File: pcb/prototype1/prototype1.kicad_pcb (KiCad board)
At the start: 2 copper layers, 95.1 x 95 mm, 98 parts, among them P1 AAA1 HOT, P2 AAA1 GND, P3 AAA2 GND, P4 AAA2 HOT, P5 USB_B, SW1 SPST, SW2 Button, SW3 Button, SW4 Button, SW5 Button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

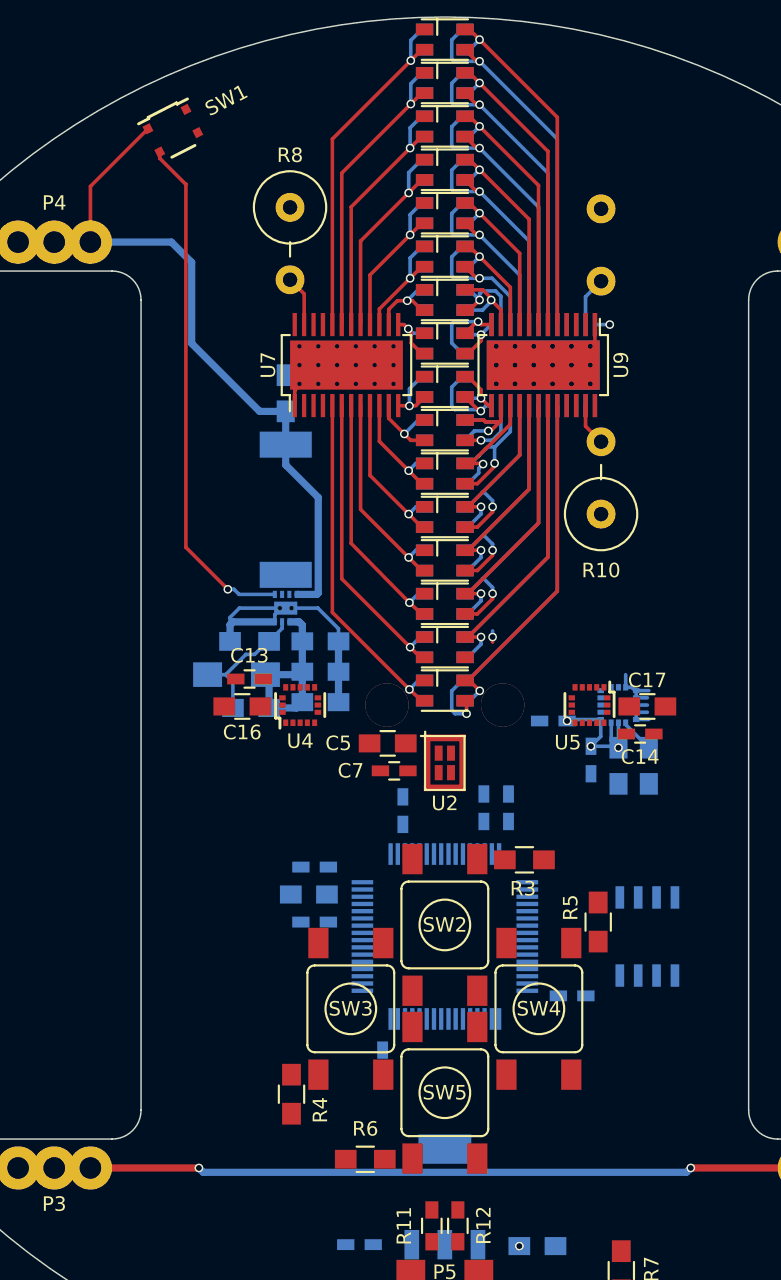
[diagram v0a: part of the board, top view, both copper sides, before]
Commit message: Change pcb layout a bit
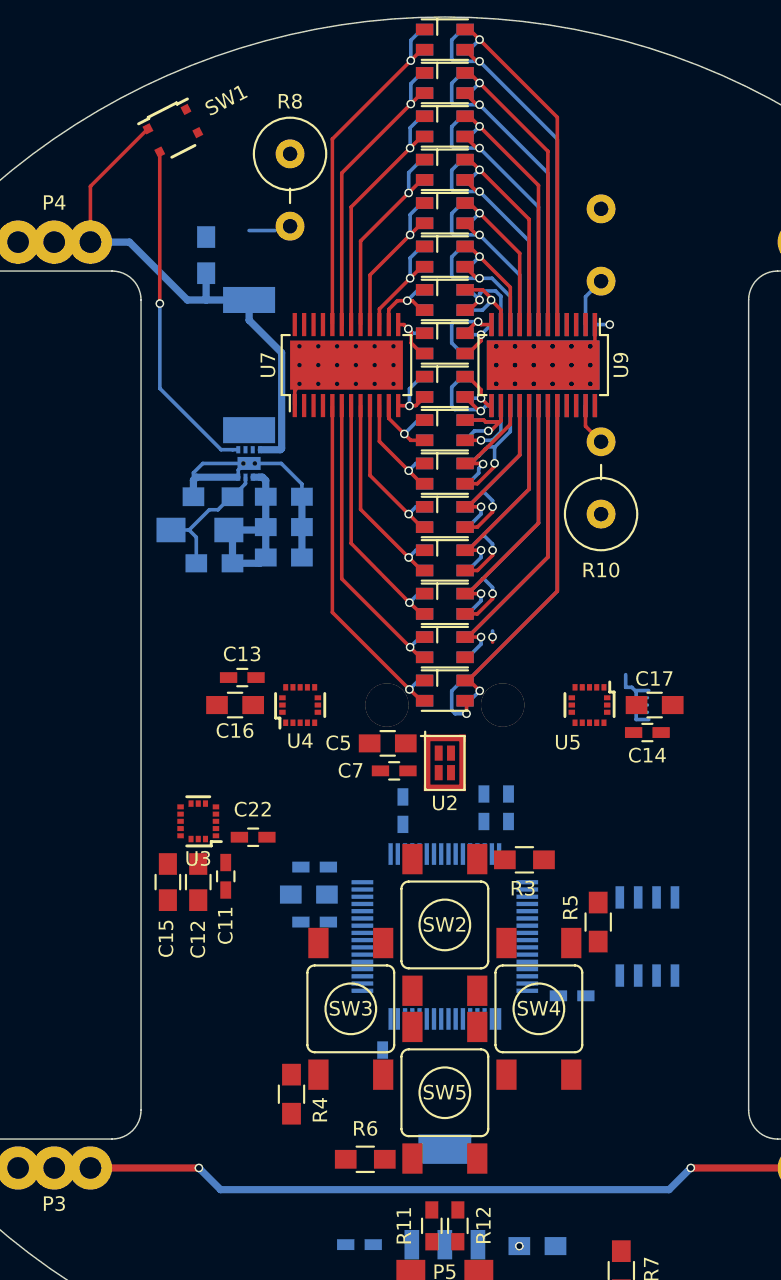
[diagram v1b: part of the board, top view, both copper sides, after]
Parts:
- C11, C12, C15, C22, U3: moved to F.Cu
- moved C15 34.2 mm to (130.9, 112.2)
- moved C12 30.1 mm to (133.0, 112.2)
- moved U3 30.1 mm to (133.0, 108.0), turned to 180 degrees
- moved C11 26.5 mm to (134.9, 111.8)
- moved C22 22.3 mm to (136.8, 109.1), turned to 0 degrees
- moved C23 11.0 mm to (133.5, 68.9)
- moved C18 10.3 mm to (134.1, 90.2)
- moved C19 10.3 mm to (138.9, 85.6)
- moved C20 10.3 mm to (138.9, 87.7)
- moved C21 10.3 mm to (138.9, 89.8)
- moved L1 10.3 mm to (136.5, 76.5)
- moved R1 10.3 mm to (133.1, 87.9)
- moved R2 10.3 mm to (134.0, 85.6)
- moved U6 10.3 mm to (136.5, 83.3)
- moved R8 3.70 mm to (139.3, 64.4)
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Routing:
- net Net-(SW1-Pad2): track 35.6 -> 23.5 mm
- net +3V3: track 25.0 -> 15.0 mm, vias 5 -> 2
- net Net-(C23-Pad2): track 45.9 -> 36.7 mm
- net Net-(R8-Pad2): track 3.50 -> 0.00 mm
- net Net-(C15-Pad1): track 2.39 -> 0.00 mm
- net Net-(P1-Pad1): track 49.2 -> 50.2 mm

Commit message: Connected many things on pcb
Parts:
- U11: footprint TO_SOT_Packages_SMD:SOT-223 -> spin:SOT-223
- moved R9 4.94 mm to (164.4, 64.9)
- moved R10 3.68 mm to (163.4, 86.9)
- moved R11 0.50 mm to (149.1, 135.5)
- moved R12 0.50 mm to (150.9, 135.5)
- turned R6 to 180 degrees
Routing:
- net LED_TOG: track 0.00 -> 191.4 mm, vias 0 -> 15
- net MISO1: track 0.47 -> 143.2 mm, vias 0 -> 11
- net SCK1: track 0.95 -> 139.7 mm, vias 0 -> 15
- net +3V3: track 15.0 -> 143.7 mm, vias 2 -> 38
- net MOSI1: track 0.48 -> 122.0 mm, vias 0 -> 11
- net SS_GREEN: track 0.00 -> 109.2 mm, vias 0 -> 11
- net SS_BLUE: track 0.00 -> 100.3 mm, vias 0 -> 12
- net SS_RED: track 0.00 -> 64.5 mm, vias 0 -> 5
- net GND: track 40.4 -> 81.2 mm, vias 2 -> 28
- net USB_DM: track 0.00 -> 28.5 mm, vias 0 -> 1
- net USB_DP: track 0.00 -> 23.8 mm, vias 0 -> 1
- net LED1: track 0.00 -> 21.0 mm, vias 0 -> 1
- net SS_GYRO: track 0.00 -> 20.0 mm, vias 0 -> 3
- net BUT2: track 0.00 -> 18.0 mm, vias 0 -> 3
- net SS_ACC2: track 0.00 -> 15.9 mm, vias 0 -> 3
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
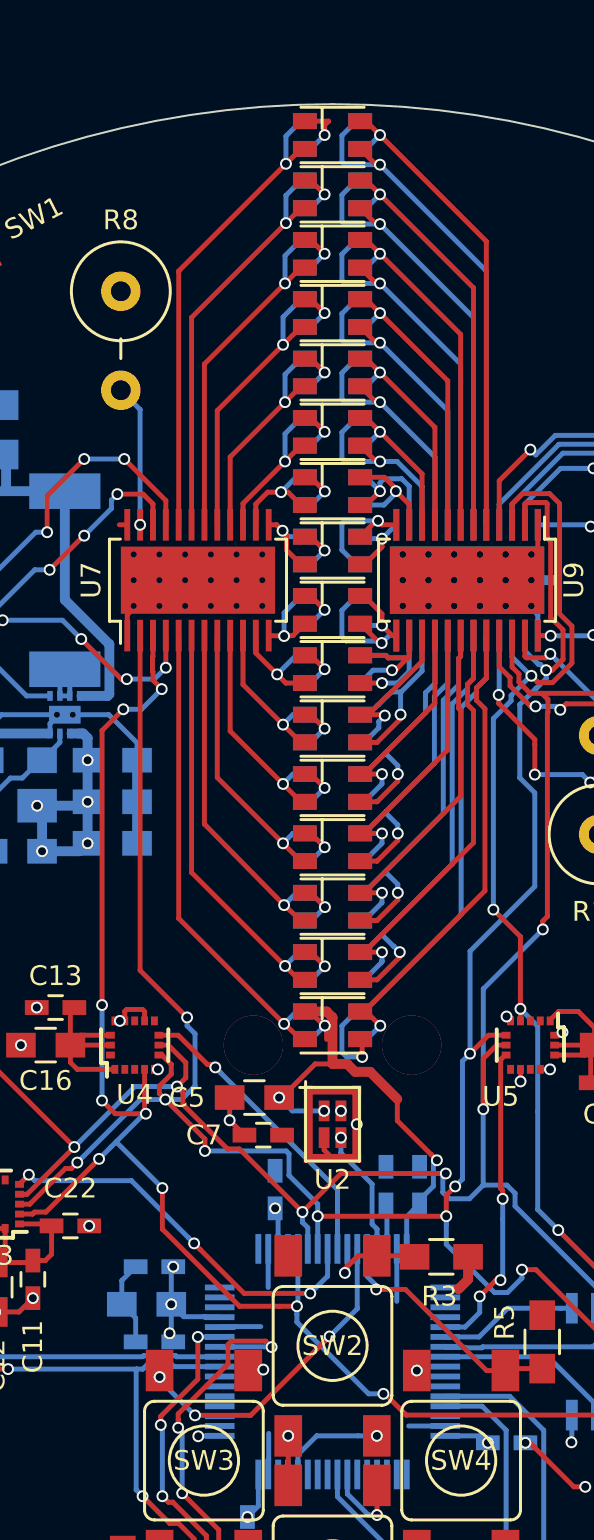
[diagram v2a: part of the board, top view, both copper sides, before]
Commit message: swap a couple pins on stm32
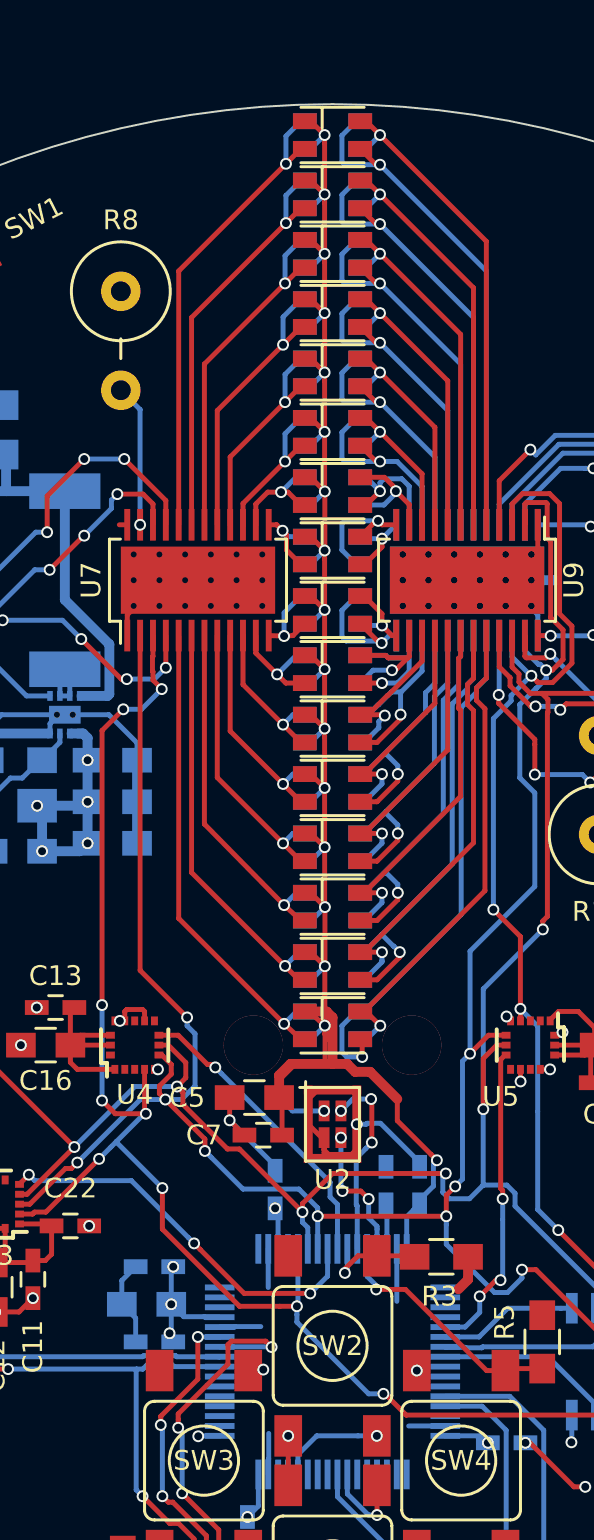
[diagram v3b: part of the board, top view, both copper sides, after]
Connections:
- U1 pad 27: BUT2 -> MIC_DATA
- U1 pad 51: MIC_DATA -> Net-(U1-Pad51)
- U1 pad 62: Net-(U1-Pad62) -> BUT2
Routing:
- net +3V3: track 143.7 -> 196.6 mm, vias 38 -> 37
- net GND: track 81.2 -> 98.2 mm
- net BUT2: track 18.0 -> 1.86 mm, vias 3 -> 0
- net MIC_DATA: track 0.00 -> 9.75 mm, vias 1 -> 3
- net MOSI1: track 122.0 -> 121.3 mm
- net MIC_CLK: track 6.38 -> 6.92 mm, vias 1 -> 3

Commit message: pcb is connected!
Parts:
- added H10: Hole, spin:Zip-tie-slot, F.Cu at (186.0, 100.0)
- added H7: Hole, spin:Zip-tie-slot, F.Cu at (132.0, 100.0)
- added H8: Hole, spin:Zip-tie-slot, F.Cu at (113.9, 100.0)
- added H9: Hole, spin:Zip-tie-slot, F.Cu at (168.0, 100.0)
- SW2, SW3, SW4, SW5: value Button -> SPST_two_terminals
- turned R3 to 180 degrees
- turned R4 to 90 degrees
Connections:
- R3 pad 1: BOOT0 -> +3V3
- R3 pad 2: +3V3 -> BUT1
- R4 pad 1: BUT2 -> +3V3
- R4 pad 2: +3V3 -> BUT2
- R6 pad 1: BUT4 -> Net-(R6-Pad1)
- SW2 pad 1: BOOT0 -> BUT1
- SW2 pad 2: GND -> BOOT0
- SW3 pad 2: GND -> Net-(SW3-Pad2)
- SW4 pad 2: GND -> Net-(SW4-Pad2)
- SW5 pad 2: GND -> Net-(R6-Pad1)
- U1 pad 26: BOOT0 -> BUT1
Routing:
- net GND: track 98.2 -> 145.5 mm, vias 28 -> 35
- net +3V3: track 196.6 -> 224.5 mm, vias 37 -> 38
- net BUT2: track 1.86 -> 12.1 mm, vias 0 -> 3
- net Net-(P1-Pad1): track 50.2 -> 60.2 mm
- net Net-(C23-Pad2): track 36.7 -> 46.5 mm
- net BUT4: track 12.5 -> 2.84 mm
- net Net-(R6-Pad1): track 0.00 -> 8.04 mm
- net BOOT0: track 10.7 -> 5.38 mm, vias 2 -> 1
- net BUT1: track 0.00 -> 5.17 mm, vias 0 -> 1
- net MISO1: track 143.4 -> 147.9 mm
- net Net-(SW1-Pad2): track 23.5 -> 28.0 mm
- net G1: track 24.7 -> 25.6 mm
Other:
- net class Default: clearance 0.2 -> 0.15
- rule trace_clearance: 0.2 -> 0.15
- rule trace_min: 0.2 -> 0.25

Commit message: Finish prototype1!!!
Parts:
- added C26: 10n, Capacitors_SMD:C_0805_HandSoldering, B.Cu at (139.3, 119.2)
- added U12: ASDMB-12.000MHZ-LC-T, spin:ASDMB-12.000MHZ-LC-T, B.Cu at (141.8, 117.8)
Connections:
- net OSC_OUT renamed Net-(U1-Pad6)
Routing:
- net GND: track 145.5 -> 155.5 mm
- net +3V3: track 224.5 -> 231.2 mm, vias 38 -> 40
- net OSC_IN: track 0.00 -> 2.14 mm
- net LED_TOG: track 191.4 -> 193.3 mm
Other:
- board text added: "BAT+"
- board text added: "BAT-"
